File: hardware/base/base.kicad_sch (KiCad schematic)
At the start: 70 parts, among them J1 SWD, J2 USB_B_Mini, J4 Serial Interface, J5 Debug, J5 OLED Display, M1 Fan_ALT, Q1 Q_NMOS_GSD, Q2 Q_NMOS_GSD, Q3 Q_NMOS_GSD, Q4 MMBT2222A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

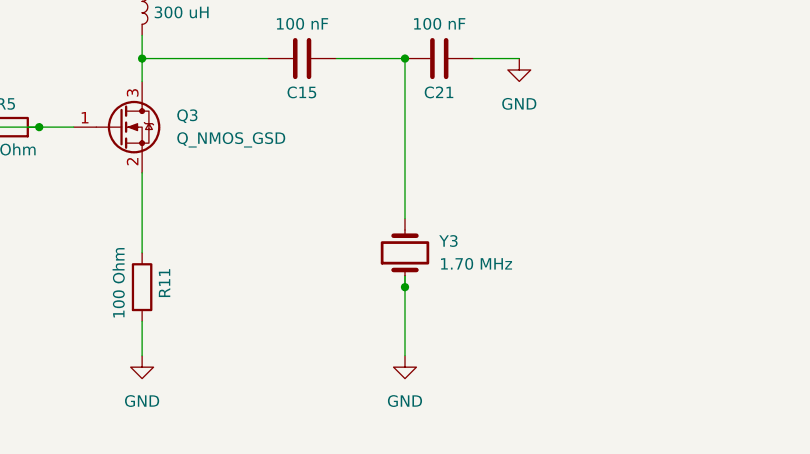
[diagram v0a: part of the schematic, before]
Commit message: Update PCB and Schema after symbol change
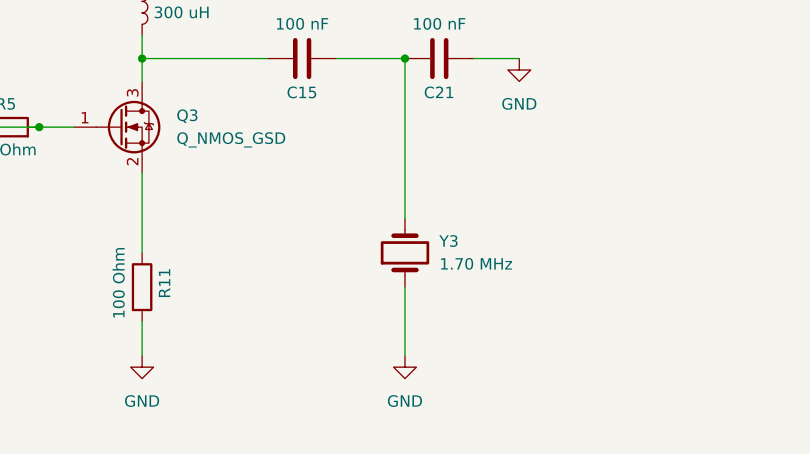
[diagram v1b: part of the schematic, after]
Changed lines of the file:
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@@
 	)
 	(junction
-		(at 276.86 233.68)
-		(diameter 0)
-		(color 0 0 0 0)
-	)
-	(junction
 		(at 342.9 45.72)
 		(diameter 0)
@@
 	(wire
 		(pts
-			(xy 276.86 233.68) (xy 276.86 241.3)
-		)
-		(stroke
-			(width 0)
-			(type default)
-		)
-	)
-	(wire
-		(pts
 			(xy 199.39 54.61) (xy 199.39 60.96)
 		)
@@
 	(wire
 		(pts
-			(xy 276.86 208.28) (xy 276.86 226.06)
-		)
-		(stroke
-			(width 0)
-			(type default)
-		)
-	)
-	(wire
-		(pts
 			(xy 116.84 153.67) (xy 119.38 153.67)
 		)
@@
 	(wire
 		(pts
-			(xy 276.86 232.41) (xy 276.86 233.68)
-		)
-		(stroke
-			(width 0)
-			(type default)
-		)
-	)
-	(wire
-		(pts
 			(xy 151.13 151.13) (xy 157.48 151.13)
 		)
@@
 	(wire
 		(pts
+			(xy 276.86 233.68) (xy 276.86 241.3)
+		)
+		(stroke
+			(width 0)
+			(type default)
+		)
+	)
+	(wire
+		(pts
 			(xy 199.39 74.93) (xy 199.39 93.98)
 		)
@@
 	(wire
 		(pts
+			(xy 276.86 208.28) (xy 276.86 226.06)
+		)
+		(stroke
+			(width 0)
+			(type default)
+		)
+	)
+	(wire
+		(pts
 			(xy 146.05 62.23) (xy 146.05 74.93)
 		)
@@
 	)
 	(symbol
+		(lib_id "Device:Crystal")
+		(at 276.86 229.87 90)
+		(unit 1)
+		(exclude_from_sim no)
+		(in_bom yes)
+		(on_board yes)
+		(dnp no)
+		(fields_autoplaced yes)
+		(property "Reference" "Y3"
+			(at 280.67 228.5999 90)
+			(effects
+				(font
+					(size 1.27 1.27)
+				)
+				(justify right)
+			)
+		)
+		(property "Value" "1.70 MHz"
+			(at 280.67 231.1399 90)
+			(effects
+				(font
+					(size 1.27 1.27)
+				)
+				(justify right)
+			)
+		)
+		(property "Footprint" "Connector_PinHeader_2.54mm:PinHeader_1x02_P2.54mm_Vertical"
+			(at 276.86 229.87 0)
+			(effects
+				(font
+					(size 1.27 1.27)
+				)
+				(hide yes)
+			)
+		)
+		(property "Datasheet" "~"
+			(at 276.86 229.87 0)
+			(effects
+				(font
+					(size 1.27 1.27)
+				)
+				(hide yes)
+			)
+		)
+		(property "Description" "Transducer"
+			(at 276.86 229.87 0)
+			(effects
+				(font
+					(size 1.27 1.27)
+				)
+				(hide yes)
+			)
+		)
+		(pin "2"
+		)
+		(pin "1"
+		)
+		(instances
+			(project "base"
+				(path "/dfe856ae-b386-4d00-a01d-c584178519be"
+					(reference "Y3")
+					(unit 1)
+				)
+			)
+		)
+	)
+	(symbol
 		(lib_id "power:GND")
 		(at 207.01 64.77 0)
@@
 					(unit 1)
 				)
-			)
-		)
-	)
-	(symbol
-		(lib_id "Device:Crystal")
-		(at 276.86 229.87 90)
-		(unit 1)
-		(exclude_from_sim no)
-		(in_bom yes)
-		(on_board yes)
-		(dnp no)
-		(fields_autoplaced yes)
-		(property "Reference" "Y3"
-			(at 280.67 228.5999 90)
-			(effects
-				(font
-					(size 1.27 1.27)
-				)
-				(justify right)
-			)
-		)
-		(property "Value" "1.70 MHz"
-			(at 280.67 231.1399 90)
-			(effects
-				(font
-					(size 1.27 1.27)
-				)
-				(justify right)
-			)
-		)
-		(property "Footprint" "Connector_PinHeader_2.54mm:PinHeader_1x02_P2.54mm_Vertical"
-			(at 276.86 229.87 0)
-			(effects
-				(font
-					(size 1.27 1.27)
-				)
-				(hide yes)
-			)
-		)
-		(property "Datasheet" "~"
-			(at 276.86 229.87 0)
-			(effects
-				(font
-					(size 1.27 1.27)
-				)
-				(hide yes)
-			)
-		)
-		(property "Description" "Transducer"
-			(at 276.86 229.87 0)
-			(effects
-				(font
-					(size 1.27 1.27)
-				)
-				(hide yes)
-			)
-		)
-		(pin "2"
-		)
-		(pin "1"
-		)
-		(instances
-			(project ""
-				(path "/dfe856ae-b386-4d00-a01d-c584178519be"
-					(reference "Y3")
-					(unit 1)
-				)

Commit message: move humidifier to fan/SD_MODE control pin, small fixes
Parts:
- removed C21: 100 nF, Capacitor_SMD:C_0603_1608Metric, symbol Device:C
- removed L1: 300 uH, Inductor_SMD:L_0603_1608Metric, symbol Device:L
- removed Q3: Q_NMOS_GSD, Package_TO_SOT_SMD:SOT-23, symbol Device:Q_NMOS_GSD
- removed R10: 10kOhm, Resistor_SMD:R_0603_1608Metric, symbol Device:R
- removed R11: 100 Ohm, Resistor_SMD:R_0603_1608Metric, symbol Device:R
- added TP3, TP5, TP6: TestPoint, E7020E:TestPoint_THTPad_1.5x1.5mm_Drill0.8mm, symbol Connector:TestPoint
- C15: value 100 nF -> 10nF
- R5: value 100 Ohm -> 10k
- R7: value 100 Ohm -> ??
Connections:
- net +3.3V: now also C16.1, J5.2 (Pin_2); no longer B1.P, C23.1, D5.1 (K)
- net AMP_BCLK: now also TP5.1
- net AMP_DIN: now also TP4.1
- net AMP_LRCLK: now also TP6.1
- net GND: now also C15.2, R5.2, U3.17 (PAD); no longer Y3.1
- net ROT_ENC_S1: now also C15.1
- net VBUS: now also C23.1, D5.1 (K), R7.1, Y3.1
- net AMP_FAN_HUM: now reaches Q2.1 (G), R6.1, RX1.1, TP2.1, U1.23 (NFC2/P0.10)
- net at M1.1 (+), Q2.3 (D): now also Y3.2
- net LED: now reaches Q1.1 (G), R2.1
- net LED: now also TP1.1, U1.32 (AIN0/P0.02); no longer Q4.1 (B), R7.2
- net HUMIDIFIER_MOSFET_GATE renamed HAPTIC
- net HAPTIC: now also Q4.1 (B), TP3.1; no longer R5.2, TP4.1
- removed net LED_HAPTIC: R7.1, TP1.1, U1.32 (AIN0/P0.02)
- new net: B1.P, R7.2
- no-connect marks 4 -> 3
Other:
- note removed: "BCLK, Serial clock, Freq = LRCLK * Bits_per_sample * Channels"
- note removed: "DIN = Serial data in"
- note removed: "Exposed Pad. The exposed pad is not internally connected. Connect the exposed page to a solid ground plane for thermal dissipation."
- note removed: "LRCLK, Left-Right clock, Freq = Audio Sample Rate"
- note removed: "Operating Voltage Range: 2.5 ~ 3.5 V_{DC}"
- note removed: "SDMODE, To GPIO if we want to be able to turn OFF"
- note removed: "http://www.learningaboutelectronics.com/Articles/Vibration-motor-circuit.php"
- moved on the sheet: B1, C10, C16, C19, C20, C23, C9, D1, D5, LS1, M1, Q1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

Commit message: finished placing components
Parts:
- removed D5: SS16, Schottky Rectifier (SS16):DIOM4325X250N, symbol Diode:SS16
- removed Q4: MMBT2222A, Package_TO_SOT_SMD:SOT-23, symbol Transistor_BJT:MMBT2222A
- added D2: D_Schottky, Schottky Diode (ZLLS500TA):SOT91P240X110-3N, symbol Device:D_Schottky
- added Q3: Q_NMOS_GSD, Package_TO_SOT_SMD:SOT-23, symbol Device:Q_NMOS_GSD
- added R10: 150 kOhm, Resistor_SMD:R_0603_1608Metric, symbol Device:R
- D3, D4: footprint Diode_SMD:D_MiniMELF -> Schottky Diode (ZLLS500TA):SOT91P240X110-3N
- R11: renamed from RX1; value 664k -> 470 kOhm
- R7: value ?? -> 22 Ohm
- R9: value 132 kOhm -> 100 kOhm
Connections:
- net +3.3V: now also D2.1 (K); no longer D3.1 (K)
- net AMP_FAN_HUM: now also R10.1; no longer R11.1
- net DETECT_VSOURCE: now also U1.32 (AIN0/P0.02); no longer U1.22 (NFC1/P0.09)
- net GND: now also Q3.2 (S)
- net HAPTIC: now also Q3.1 (G)
- net LED: now also U1.22 (NFC1/P0.09); no longer U1.32 (AIN0/P0.02)
- net VBUS: now also D3.1 (K)
- net at R7.2: now also B1.1; no longer B1.P
- net at C23.2: now also B1.2, D3.2 (A), Q3.3 (D); no longer B1.N
- net at BT1.1 (+): now also D2.2 (A); no longer D3.2 (A)
- new net: R10.2, R11.1
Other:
- note removed: "3.3/5 = (132)/(68+132)"
- note removed: "Divide voltage to get 3.3V from 5V"
- note removed: "V_{out}= V_{in} * (R_{2})/(R_{1}+R_{2})"
- moved on the sheet: R5, R7, TP2, TP3

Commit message: Finish front layer traces
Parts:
- removed D2, D3, D4: D_Schottky, Schottky Diode (ZLLS500TA):SOT91P240X110-3N, symbol Device:D_Schottky
- added D2, D3, D4: D_Schottky_1_3, Schottky Diode (ZLLS500TA):SOT91P240X110-3N, symbol SOT91P240X110-3N:D_Schottky_1_3
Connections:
- net +3.3V: now also D2.3 (K), D3.3 (K)
- net VBUS: now also D4.3 (K)
- net at BT1.1 (+): now also D2.1 (A)
- net at B1.2, C23.2, Q3.3 (D): now also D4.1 (A)
- net at C25.1, U4.3 (VO): now also D3.1 (A)
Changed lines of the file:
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@@
 	)
 	(symbol
-		(lib_id "Device:D_Schottky")
-		(at 87.63 236.22 180)
+		(lib_id "power:GND")
+		(at 132.08 55.88 0)
 		(unit 1)
 		(exclude_from_sim no)
@@
 		(on_board yes)
 		(dnp no)
-		(fields_autoplaced yes)
-		(property "Reference" "D2"
-			(at 87.9475 229.87 0)
+		(property "Reference" "#PWR014"
+			(at 132.08 62.23 0)
 			(effects
 				(font
 					(size 1.27 1.27)
 				)
+				(hide yes)
 			)
 		)
-		(property "Value" "D_Schottky"
-			(at 87.9475 232.41 0)
+		(property "Value" "GND"
+			(at 132.08 60.452 0)
 			(effects
 				(font
@@
 			)
 		)
-		(property "Footprint" "Schottky Diode (ZLLS500TA):SOT91P240X110-3N"
-			(at 87.63 236.22 0)
+		(property "Footprint" ""
+			(at 132.08 55.88 0)
 			(effects
 				(font
@@
 			)
 		)
-		(property "Datasheet" "~"
-			(at 87.63 236.22 0)
+		(property "Datasheet" ""
+			(at 132.08 55.88 0)
 			(effects
 				(font
@@
 			)
 		)
-		(property "Description" "Schottky diode"
-			(at 87.63 236.22 0)
+		(property "Description" "Power symbol creates a global label with name \"GND\" , ground"
+			(at 132.08 55.88 0)
 			(effects
 				(font
@@
 		(pin "1"
 		)
-		(pin "2"
-		)
 		(instances
+			(project "baseboard"
+				(path "/aee89fc2-a1fb-42cc-8710-cdded9bcb32a"
+					(reference "#PWR014")
+					(unit 1)
+				)
+			)
 			(project "base"
 				(path "/dfe856ae-b386-4d00-a01d-c584178519be"
-					(reference "D2")
+					(reference "#PWR0104")
 					(unit 1)
 				)
@@
 	)
 	(symbol
-		(lib_id "power:GND")
-		(at 132.08 55.88 0)
+		(lib_id "SOT91P240X110-3N:D_Schottky_1_3")
+		(at 87.63 236.22 180)
 		(unit 1)
 		(exclude_from_sim no)
@@
 		(on_board yes)
 		(dnp no)
-		(property "Reference" "#PWR014"
-			(at 132.08 62.23 0)
+		(fields_autoplaced yes)
+		(property "Reference" "D2"
+			(at 87.9475 229.87 0)
 			(effects
 				(font
 					(size 1.27 1.27)
 				)
-				(hide yes)
 			)
 		)
-		(property "Value" "GND"
-			(at 132.08 60.452 0)
+		(property "Value" "D_Schottky_1_3"
+			(at 87.9475 232.41 0)
 			(effects
 				(font
@@
 			)
 		)
-		(property "Footprint" ""
-			(at 132.08 55.88 0)
+		(property "Footprint" "Schottky Diode (ZLLS500TA):SOT91P240X110-3N"
+			(at 87.63 236.22 0)
 			(effects
 				(font
@@
 			)
 		)
-		(property "Datasheet" ""
-			(at 132.08 55.88 0)
+		(property "Datasheet" "~"
+			(at 87.63 236.22 0)
 			(effects
 				(font
@@
 			)
 		)
-		(property "Description" "Power symbol creates a global label with name \"GND\" , ground"
-			(at 132.08 55.88 0)
+		(property "Description" "Schottky diode"
+			(at 87.63 236.22 0)
 			(effects
 				(font
@@
 		(pin "1"
 		)
+		(pin "3"
+		)
 		(instances
-			(project "baseboard"
-				(path "/aee89fc2-a1fb-42cc-8710-cdded9bcb32a"
-					(reference "#PWR014")
-					(unit 1)
-				)
-			)
 			(project "base"
 				(path "/dfe856ae-b386-4d00-a01d-c584178519be"
-					(reference "#PWR0104")
+					(reference "D2")
 					(unit 1)
 				)
@@
 	)
 	(symbol
+		(lib_id "SOT91P240X110-3N:D_Schottky_1_3")
+		(at 265.43 36.83 270)
+		(unit 1)
+		(exclude_from_sim no)
+		(in_bom yes)
+		(on_board yes)
+		(dnp no)
+		(property "Reference" "D4"
+			(at 248.158 35.052 90)
+			(effects
+				(font
+					(size 1.27 1.27)
+				)
+				(justify left)
+			)
+		)
+		(property "Value" "D_Schottky_1_3"
+			(at 248.158 37.592 90)
+			(effects
+				(font
+					(size 1.27 1.27)
+				)
+				(justify left)
+			)
+		)
+		(property "Footprint" "Schottky Diode (ZLLS500TA):SOT91P240X110-3N"
+			(at 265.43 36.83 0)
+			(effects
+				(font
+					(size 1.27 1.27)
+				)
+				(hide yes)
+			)
+		)
+		(property "Datasheet" "~"
+			(at 265.43 36.83 0)
+			(effects
+				(font
+					(size 1.27 1.27)
+				)
+				(hide yes)
+			)
+		)
+		(property "Description" "Schottky diode"
+			(at 265.43 36.83 0)
+			(effects
+				(font
+					(size 1.27 1.27)
+				)
+				(hide yes)
+			)
+		)
+		(pin "1"
+		)
+		(pin "3"
+		)
+		(instances
+			(project "base"
+				(path "/dfe856ae-b386-4d00-a01d-c584178519be"
+					(reference "D4")
+					(unit 1)
+				)
+			)
+		)
+	)
+	(symbol
 		(lib_id "Device:C")
 		(at 212.09 109.22 180)
@@
 	)
 	(symbol
+		(lib_id "SOT91P240X110-3N:D_Schottky_1_3")
+		(at 87.63 215.9 180)
+		(unit 1)
+		(exclude_from_sim no)
+		(in_bom yes)
+		(on_board yes)
+		(dnp no)
+		(fields_autoplaced yes)
+		(property "Reference" "D3"
+			(at 87.9475 209.55 0)
+			(effects
+				(font
+					(size 1.27 1.27)
+				)
+			)
+		)
+		(property "Value" "D_Schottky_1_3"
+			(at 87.9475 212.09 0)
+			(effects
+				(font
+					(size 1.27 1.27)
+				)
+			)
+		)
+		(property "Footprint" "Schottky Diode (ZLLS500TA):SOT91P240X110-3N"
+			(at 87.63 215.9 0)
+			(effects
+				(font
+					(size 1.27 1.27)
+				)
+				(hide yes)
+			)
+		)
+		(property "Datasheet" "~"
+			(at 87.63 215.9 0)
+			(effects
+				(font
+					(size 1.27 1.27)
+				)
+				(hide yes)
+			)
+		)
+		(property "Description" "Schottky diode"
+			(at 87.63 215.9 0)
+			(effects
+				(font
+					(size 1.27 1.27)
+				)
+				(hide yes)
+			)
+		)
+		(pin "1"
+		)
+		(pin "3"
+		)
+		(instances
+			(project "base"
+				(path "/dfe856ae-b386-4d00-a01d-c584178519be"
+					(reference "D3")
+					(unit 1)
+				)
+			)
+		)
+	)
+	(symbol
 		(lib_id "Device:C")
 		(at 313.69 133.35 0)
@@
 	)
 	(symbol
-		(lib_id "Device:D_Schottky")
-		(at 265.43 36.83 270)
-		(unit 1)
-		(exclude_from_sim no)
-		(in_bom yes)
-		(on_board yes)
-		(dnp no)
-		(fields_autoplaced yes)
-		(property "Reference" "D3"
-			(at 267.97 35.2424 90)
-			(effects
-				(font
-					(size 1.27 1.27)
-				)
-				(justify left)
-			)
-		)
-		(property "Value" "D_Schottky"
-			(at 267.97 37.7824 90)
-			(effects
-				(font
-					(size 1.27 1.27)
-				)
-				(justify left)
-			)
-		)
-		(property "Footprint" "Schottky Diode (ZLLS500TA):SOT91P240X110-3N"
-			(at 265.43 36.83 0)
-			(effects
-				(font
-					(size 1.27 1.27)
-				)
-				(hide yes)
-			)
-		)
-		(property "Datasheet" "~"
-			(at 265.43 36.83 0)
-			(effects
-				(font
-					(size 1.27 1.27)
-				)
-				(hide yes)
-			)
-		)
-		(property "Description" "Schottky diode"
-			(at 265.43 36.83 0)
-			(effects
-				(font
-					(size 1.27 1.27)
-				)
-				(hide yes)
-			)
-		)
-		(pin "1"
-		)
-		(pin "2"
-		)
-		(instances
-			(project "base"
-				(path "/dfe856ae-b386-4d00-a01d-c584178519be"
-					(reference "D3")
-					(unit 1)
-				)
-			)
-		)
-	)
-	(symbol
 		(lib_id "Device:C")
 		(at 176.53 78.74 0)
@@
 					(unit 1)
 				)
-			)
-		)
-	)
-	(symbol
-		(lib_id "Device:D_Schottky")
-		(at 87.63 215.9 180)
-		(unit 1)
-		(exclude_from_sim no)
-		(in_bom yes)
-		(on_board yes)
-		(dnp no)
-		(fields_autoplaced yes)
-		(property "Reference" "D4"
-			(at 87.9475 209.55 0)
-			(effects
-				(font
-					(size 1.27 1.27)
-				)
-			)
-		)
-		(property "Value" "D_Schottky"
-			(at 87.9475 212.09 0)
-			(effects
-				(font
-					(size 1.27 1.27)
-				)
-			)
-		)
-		(property "Footprint" "Schottky Diode (ZLLS500TA):SOT91P240X110-3N"
-			(at 87.63 215.9 0)
-			(effects
-				(font
-					(size 1.27 1.27)
-				)
-				(hide yes)
-			)
-		)
-		(property "Datasheet" "~"
-			(at 87.63 215.9 0)
-			(effects
-				(font
-					(size 1.27 1.27)
-				)
-				(hide yes)
-			)
-		)
-		(property "Description" "Schottky diode"
-			(at 87.63 215.9 0)
-			(effects
-				(font
-					(size 1.27 1.27)
-				)
-				(hide yes)
-			)
-		)
-		(pin "1"
-		)
-		(pin "2"
-		)
-		(instances
-			(project "base"
-				(path "/dfe856ae-b386-4d00-a01d-c584178519be"
-					(reference "D4")
-					(unit 1)
-				)

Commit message: add mounting holes
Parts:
- added H1, H2, H3, H4: MountingHole, MountingHole:MountingHole_2.2mm_M2_ISO7380, symbol Mechanical:MountingHole

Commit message: Add pull-up resistors to display
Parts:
- added R12, R13: 10k, Resistor_SMD:R_0603_1608Metric, symbol Device:R
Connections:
- net +3.3V: now also R12.1, R13.1
- net at J5.4 (Pin_4), U1.6 (P1.09): now also R12.2
- net at J5.3 (Pin_3), U1.7 (P0.11): now also R13.2
